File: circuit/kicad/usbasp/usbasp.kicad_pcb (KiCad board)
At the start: 2 copper layers, 47.3 x 25 mm, 23 parts, among them J1 Conn_01x06_Male, J2 USB_B_Micro, SW1 SW_Push, SW2 SW_Push, U1 ATmega8A-A, Y1 Crystal

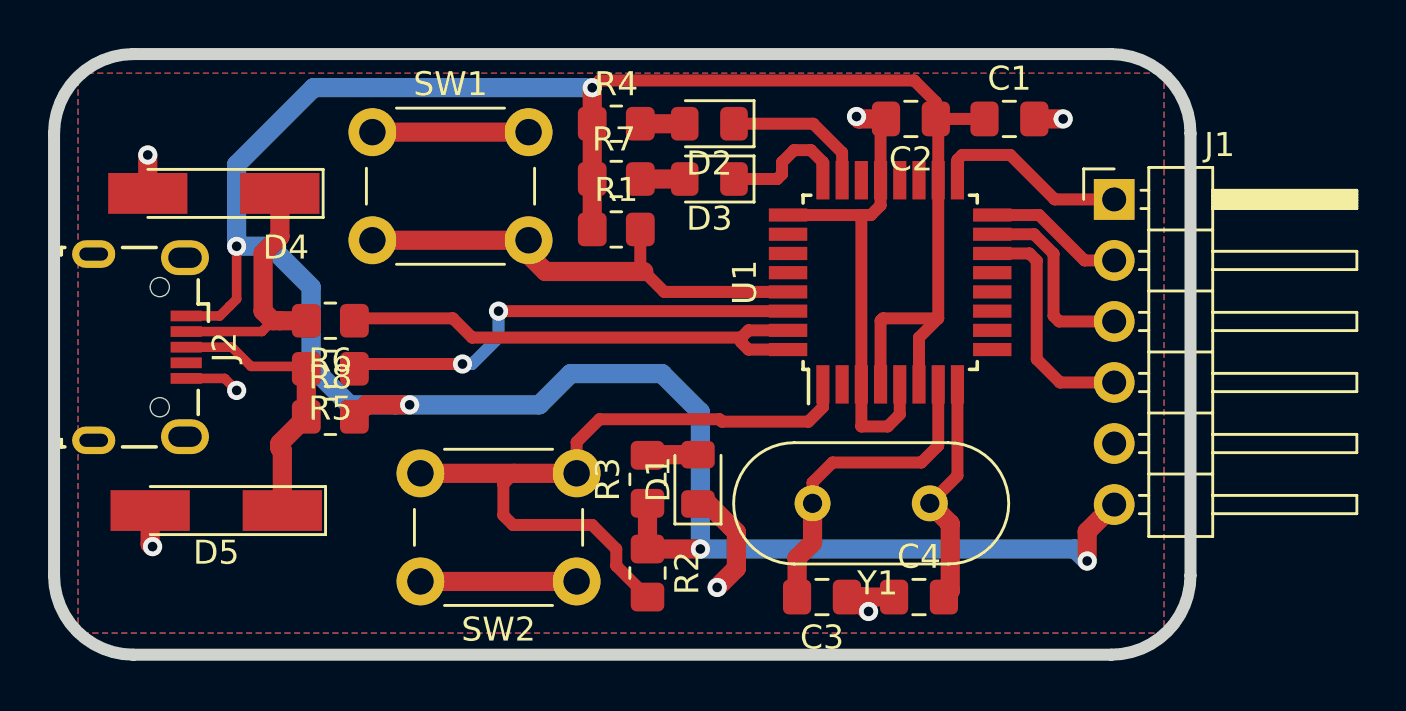
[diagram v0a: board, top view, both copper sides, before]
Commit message: Migrate Eagle-KiCAD
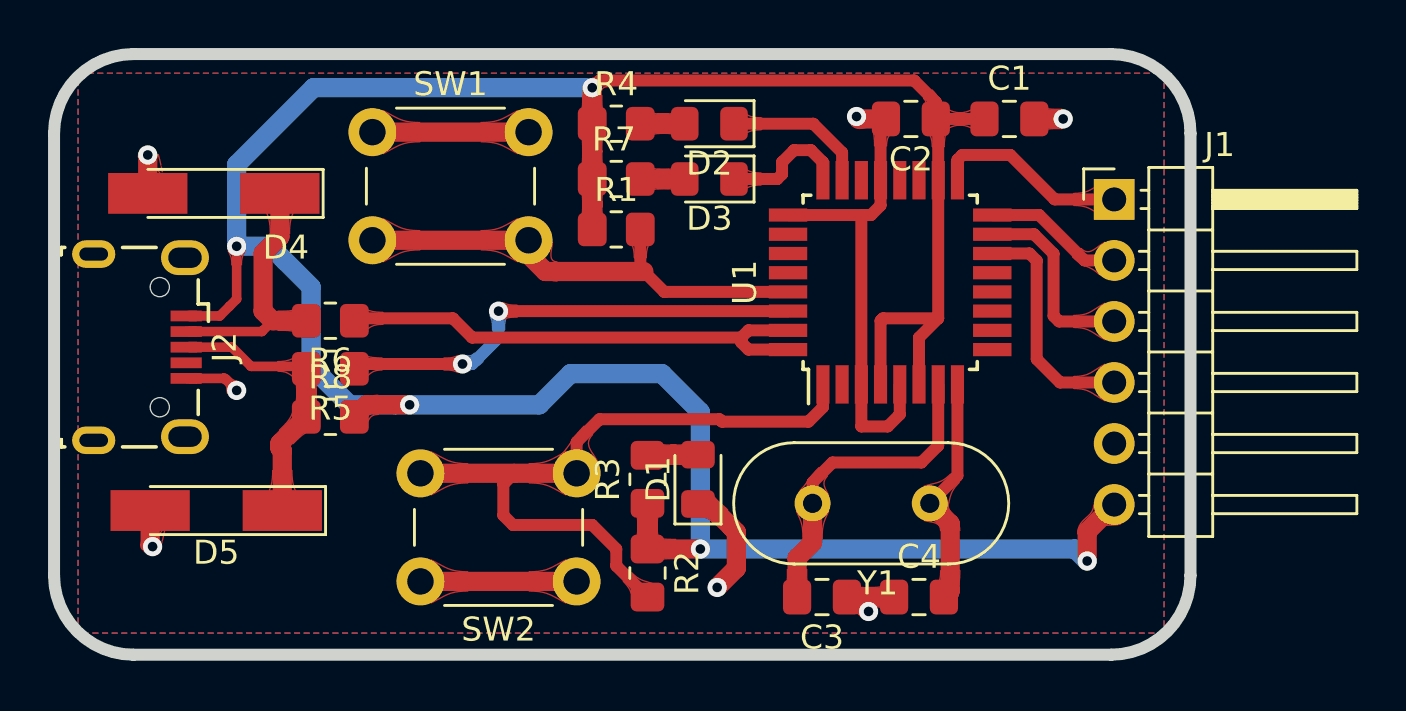
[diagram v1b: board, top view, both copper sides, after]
